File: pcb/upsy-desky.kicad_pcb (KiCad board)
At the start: 2 copper layers, 40.9 x 58 mm, 48 parts, among them J1 RJ45, J2 RJ45, J3 USB_C_ReceptacleUSB2.0, Q1 MMBT3904, Q2 MMBT3904, Q3 BSS138, Q4 BSS138, Q5 BSS138, Q6 BSS138, Q7 BSS138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

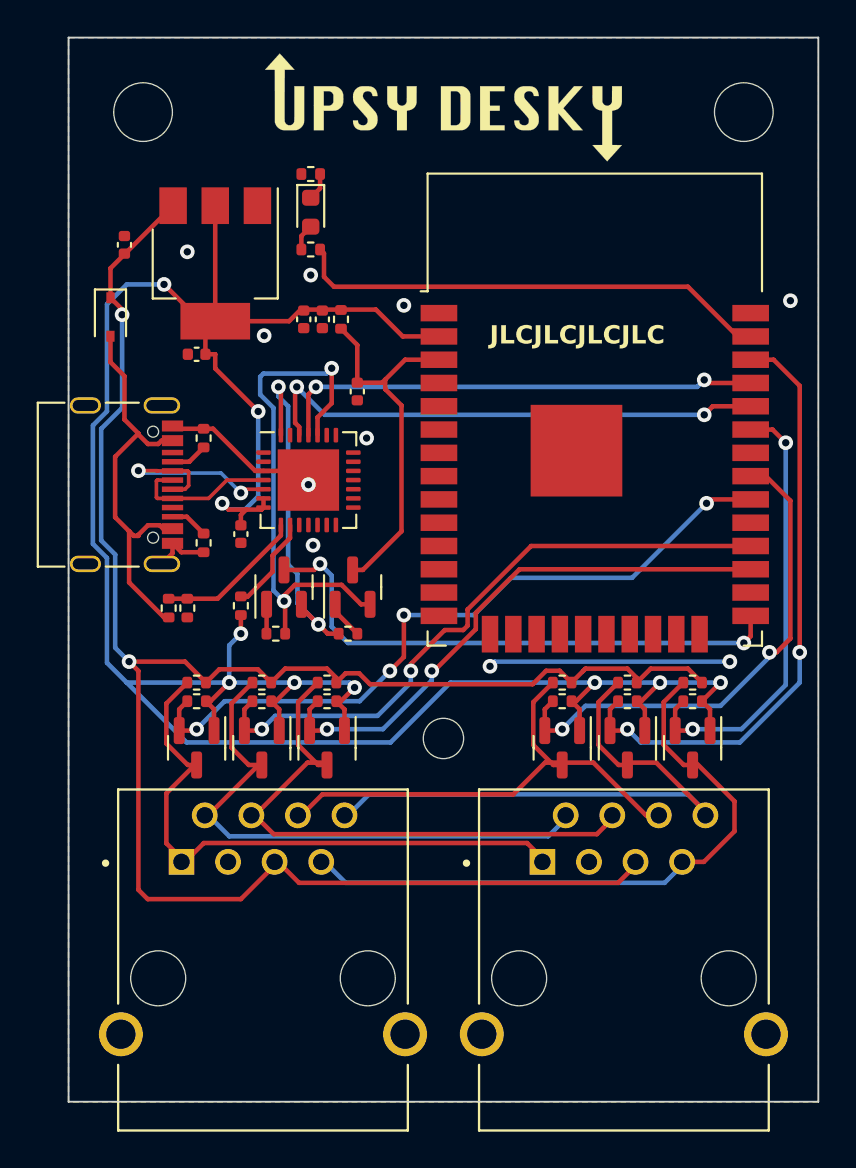
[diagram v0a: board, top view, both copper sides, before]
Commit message: Adding updated PCB files using ESP32-s3-WROOM-1 MCU, removed UART to USB logic
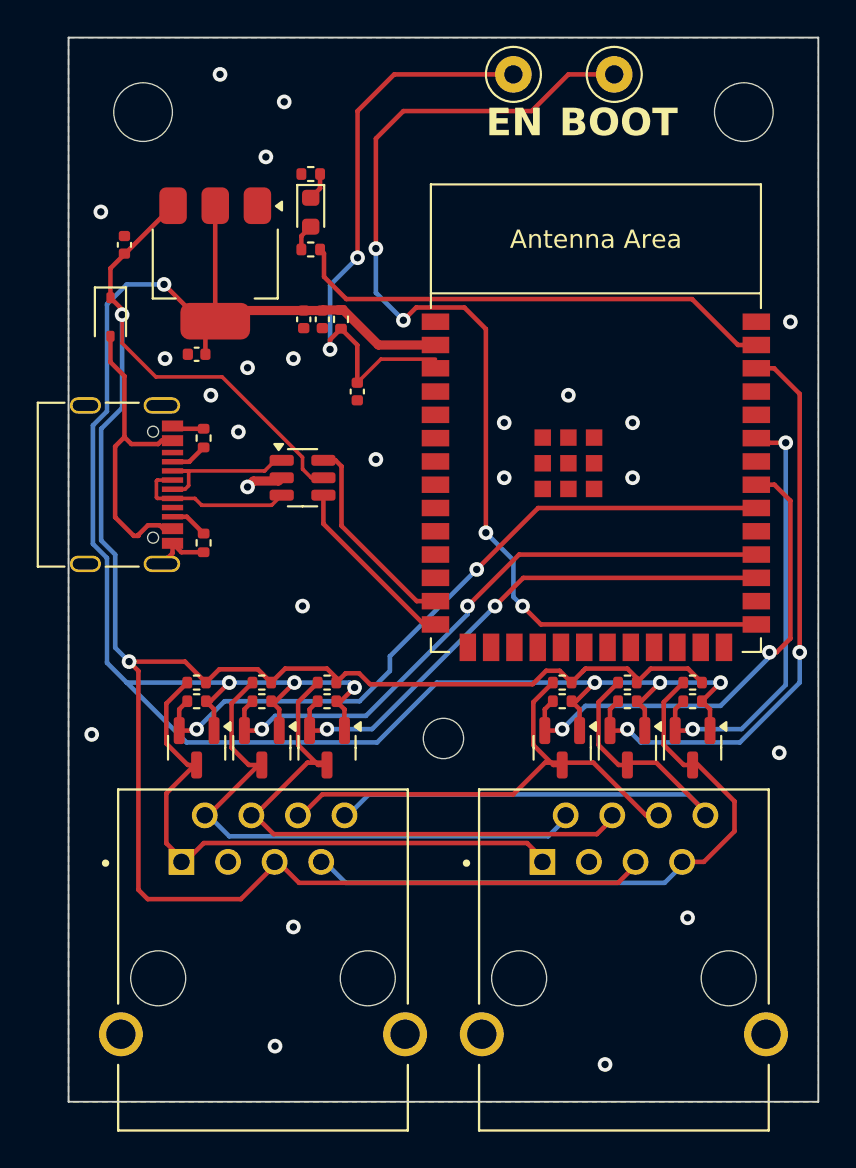
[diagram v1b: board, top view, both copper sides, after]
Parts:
- removed C6: 10u, Capacitor_SMD:C_0402_1005Metric
- removed Q1, Q2: MMBT3904, Package_TO_SOT_SMD:SOT-23
- removed R18: 1k, Resistor_SMD:R_0402_1005Metric
- removed R19: 22.1k, Resistor_SMD:R_0402_1005Metric
- removed R20: 47.5k, Resistor_SMD:R_0402_1005Metric
- removed R3, R4: 10k, Resistor_SMD:R_0402_1005Metric
- removed Ref**: Val**, footprints:dark_logotype_horizontal
- removed U3: ESP32-WROOM-32, RF_Module:ESP32-WROOM-32
- added TP1: TestPoint, TestPoint:TestPoint_Loop_D1.80mm_Drill1.0mm_Beaded, F.Cu at (156.0, 73.0)
- added TP2: TestPoint, TestPoint:TestPoint_Loop_D1.80mm_Drill1.0mm_Beaded, F.Cu at (150.5, 73.0)
- added U4: ESP32-S3-WROOM-1, PCM_Espressif:ESP32-S3-WROOM-1, F.Cu at (155.0, 94.8)
- D1: value 1N5817 -> 1N5819WS
- Q3, Q4, Q5, Q6, Q7, Q8: value BSS138 -> 2N7002
- U1: value CP2102N-Axx-xQFN28 -> USBLC6-2SC6; footprint Package_DFN_QFN:QFN-28-1EP_5x5mm_P0.5mm_EP3.35x3.35mm -> Package_TO_SOT_SMD:SOT-23-6
- moved U1 0.34 mm to (139.0, 95.0)
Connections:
- net /EN renamed /MCU/EN
- J3 pad A6: /USB_D+ -> /USB_HDR_P
- J3 pad A7: /USB_D- -> /USB_HDR_N
- J3 pad B6: /USB_D+ -> /USB_HDR_P
- J3 pad B7: /USB_D- -> /USB_HDR_N
- U1 pad 1: unconnected-(U1-Pad1) -> /USB_HDR_N
- U1 pad 2: unconnected-(U1-Pad2) -> GND
- U1 pad 3: GND -> /USB_HDR_P
- U1 pad 4: /USB_D+ -> /USB_P
- U1 pad 5: /USB_D- -> +5V
- U1 pad 6: +3V3 -> /USB_N
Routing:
- net Net-(U4-GPIO0/BOOT): track 0.00 -> 59.4 mm, vias 0 -> 4
- net /GPIO0: track 30.3 -> 0.00 mm, vias 2 -> 0
- net /ESP_RX: track 28.3 -> 0.00 mm, vias 2 -> 0
- net /RTS: track 28.3 -> 0.00 mm, vias 2 -> 0
- net /ESP_TX: track 26.7 -> 0.00 mm, vias 2 -> 0
- net /DTR: track 19.6 -> 0.00 mm, vias 2 -> 0
- net +3V3: track 136.7 -> 118.1 mm, vias 10 -> 7
- net GND: track 24.9 -> 7.11 mm, vias 10 -> 24
- net +5V: track 105.1 -> 121.1 mm
- net /MCU/EN: track 19.5 -> 32.4 mm, vias 0 -> 2
- net /USB_D-: track 11.9 -> 0.00 mm, vias 2 -> 0
- net /USB_N: track 0.00 -> 11.2 mm
- net /USB_P: track 0.00 -> 9.95 mm
- net /USB_HDR_P: track 0.00 -> 9.04 mm
- net /USB_HDR_N: track 0.00 -> 8.81 mm
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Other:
- board text added: "Andrew DeMartino Smart Desk Rev. A 11/17/24"
- board text added: "BOOT"
- board text added: "EN"
- board text removed: "JLCJLCJLCJLC"
